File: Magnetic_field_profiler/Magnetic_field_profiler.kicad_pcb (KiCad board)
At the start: 4 copper layers, 92 x 37 mm, 71 parts, among them J1 USB_B_Micro, J2 Barrel_Jack_Switch, J3 Conn_01x04_Socket, Q1 BSS123, SW1 SW_SPDT, U1 STM32F103C8Tx, U10 MLX90393, U11 MLX90393, U12 MLX90393, U2 AP2112K-3.3, U3 DRV8825, U4 MLX90393, U5 MLX90393, U6 MLX90393, U7 MLX90393, U8 MLX90393, U9 MLX90393, Y1 Crystal_GND24

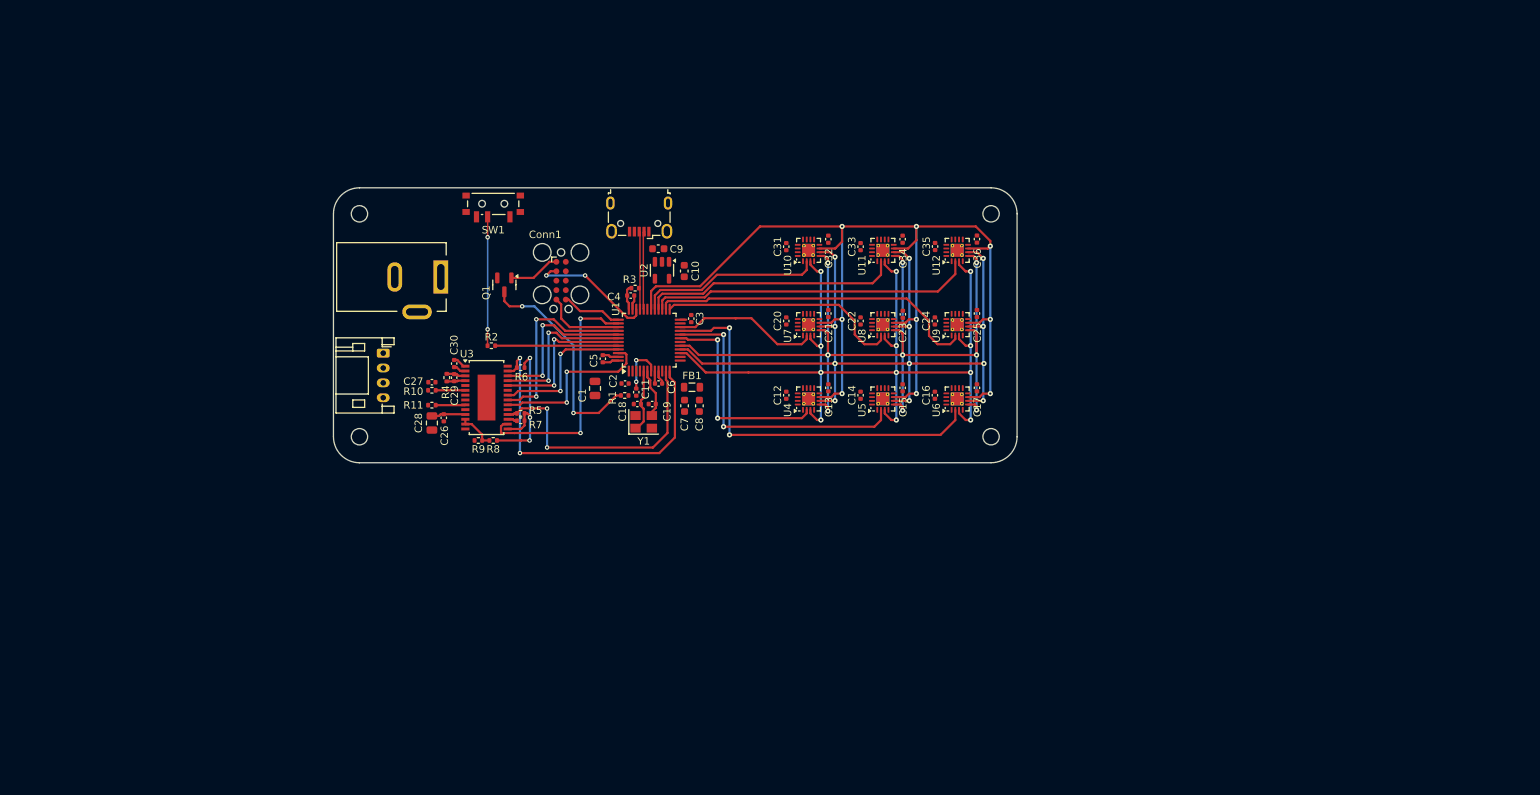
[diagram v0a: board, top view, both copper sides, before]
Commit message: SMPS Added, Edge Cuts Modified
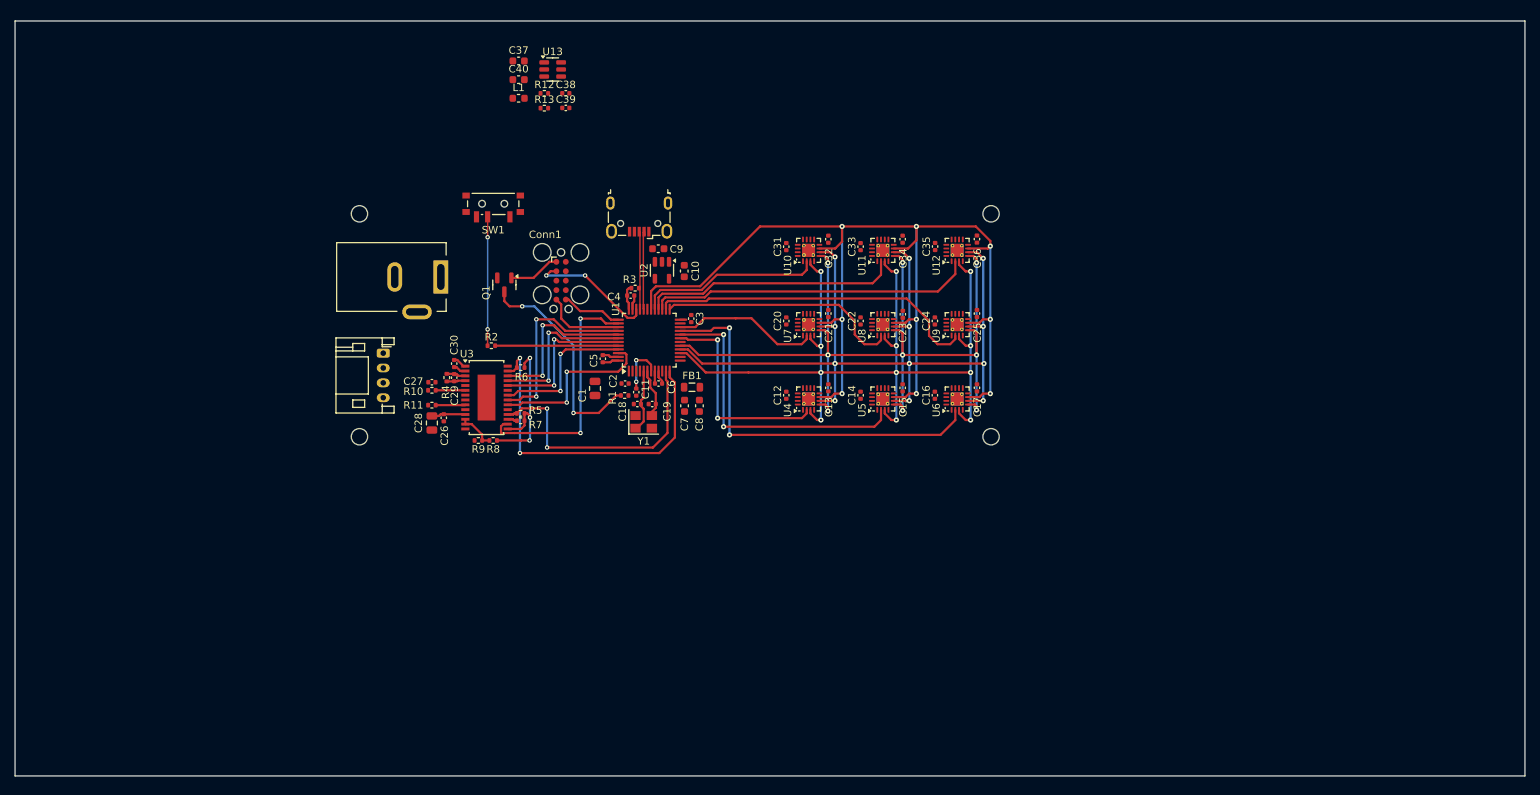
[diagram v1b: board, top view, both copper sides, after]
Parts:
- added C37: 22u, Capacitor_SMD:C_0603_1608Metric, F.Cu at (93.2, 56.2)
- added C38: 100n, Capacitor_SMD:C_0402_1005Metric, F.Cu at (99.5, 60.5)
- added C39: 100n, Capacitor_SMD:C_0402_1005Metric, F.Cu at (99.5, 62.5)
- added C40: 22u, Capacitor_SMD:C_0603_1608Metric, F.Cu at (93.2, 58.7)
- added L1: 100u, Inductor_SMD:L_0603_1608Metric, F.Cu at (93.2, 61.2)
- added R12: R, Resistor_SMD:R_0402_1005Metric, F.Cu at (96.6, 60.5)
- added R13: R, Resistor_SMD:R_0402_1005Metric, F.Cu at (96.6, 62.5)
- added U13: TP6841S6, Package_TO_SOT_SMD:SOT-23-6, F.Cu at (97.8, 57.3)
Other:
- board size 92 x 37 mm -> 203.2 x 101.6 mm

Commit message: Edge cuts updated
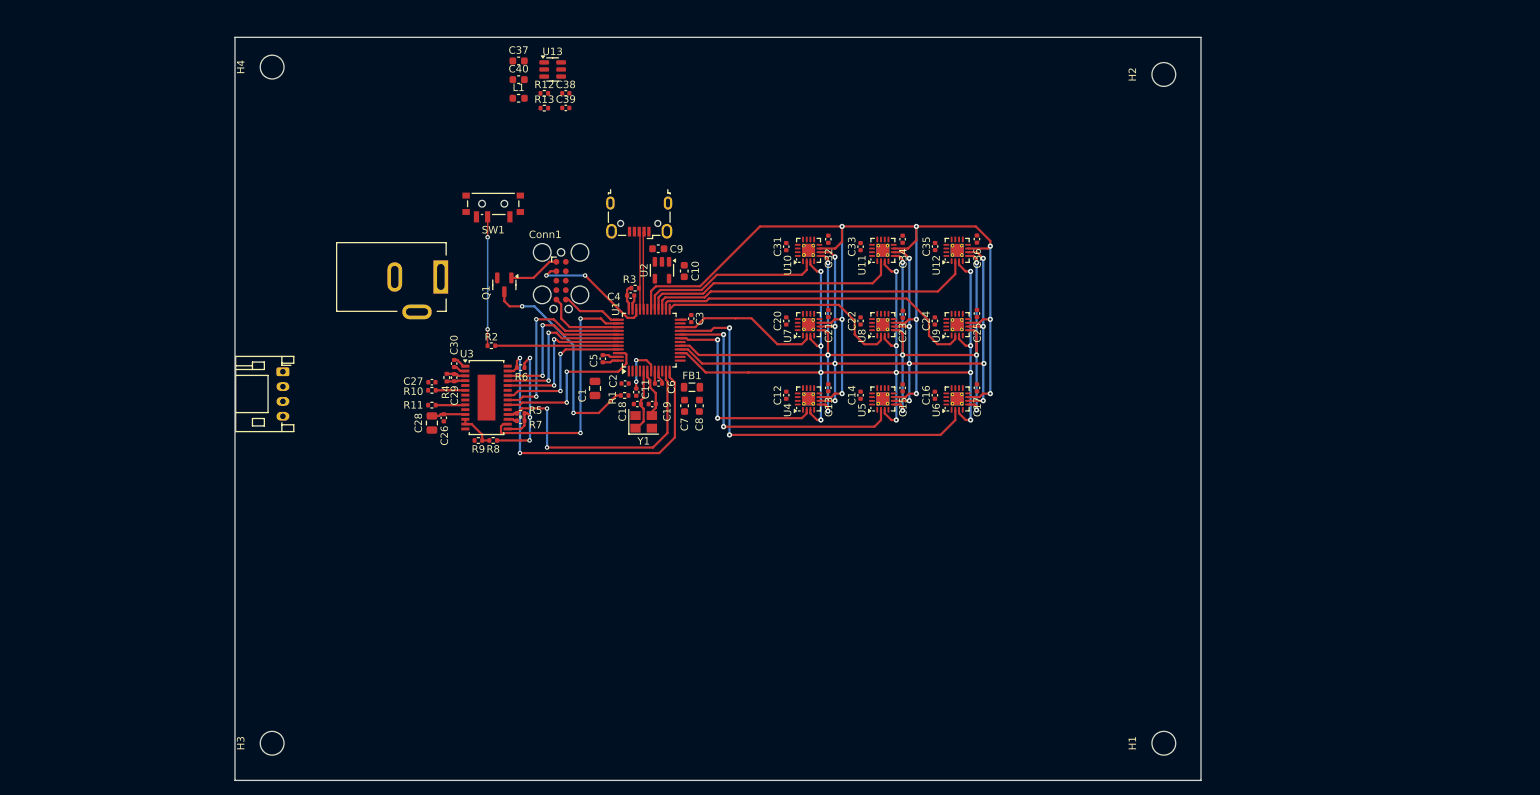
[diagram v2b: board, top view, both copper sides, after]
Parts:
- H1, H2, H3, H4: footprint MountingHole:MountingHole_2.2mm_M2 -> MountingHole:MountingHole_3.2mm_M3
- R12: value R -> 75k
- R13: value R -> 24k
- moved H1 47.4 mm to (180.0, 148.0)
- moved H3 42.9 mm to (60.0, 148.0)
- moved H2 29.9 mm to (180.0, 58.0)
- moved H4 23.0 mm to (60.0, 57.0)
- moved J3 13.7 mm to (61.5, 98.0)
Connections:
- C26 pad 1: +24V -> +12V
- C27 pad 1: +24V -> +12V
- C28 pad 1: +24V -> +12V
- C29 pad 1: +24V -> +12V
- R4 pad 1: +24V -> +12V
- U3 pad 11: +24V -> +12V
- U3 pad 4: +24V -> +12V
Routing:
- net +24V: track 7.15 -> 0.00 mm
- net +12V: track 0.00 -> 7.15 mm
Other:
- board size 203.2 x 101.6 mm -> 130 x 100 mm

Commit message: PCB Updates and Second Motor Support
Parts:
- added C41: 100n, Capacitor_SMD:C_0402_1005Metric, F.Cu at (142.4, 121.5)
- added C42: 100n, Capacitor_SMD:C_0402_1005Metric, F.Cu at (152.5, 126.8)
- added C43: 100n, Capacitor_SMD:C_0402_1005Metric, F.Cu at (152.5, 128.8)
- added J4: Screw_Terminal_01x06, TerminalBlock:TerminalBlock_Xinya_XY308-2.54-6P_1x06_P2.54mm_Horizontal, F.Cu at (60.0, 70.3)
- added R14: 1M, Resistor_SMD:R_0402_1005Metric, F.Cu at (119.5, 112.3)
- added R15: 10k, Resistor_SMD:R_0402_1005Metric, F.Cu at (119.5, 114.3)
- added R16: 10k, Resistor_SMD:R_0402_1005Metric, F.Cu at (119.5, 116.3)
- added R17: 10k, Resistor_SMD:R_0402_1005Metric, F.Cu at (119.5, 118.3)
- added R18: 50k, Resistor_SMD:R_0402_1005Metric, F.Cu at (119.5, 120.2)
- added R19: 30k, Resistor_SMD:R_0402_1005Metric, F.Cu at (119.5, 122.2)
- added R20: 200m, Resistor_SMD:R_0402_1005Metric, F.Cu at (119.5, 124.2)
- added R21: 200m, Resistor_SMD:R_0402_1005Metric, F.Cu at (119.5, 126.2)
- C10, C9: value 1u -> 100n; footprint Capacitor_SMD:C_0603_1608Metric -> Capacitor_SMD:C_0402_1005Metric
- C14: value 100n -> 100u; footprint Capacitor_SMD:C_0402_1005Metric -> Capacitor_SMD:C_0805_2012Metric
- C16: value 100n -> 10n
- J2: value Barrel_Jack_Switch -> Conn_01x04_Socket; footprint Connector_BarrelJack:BarrelJack_Kycon_KLDX-0202-xC_Horizontal -> Connector_JST:JST_PH_S4B-PH-K_1x04_P2.00mm_Horizontal
- U2: value AP2112K-3.3 -> MLX90393; footprint Package_TO_SOT_SMD:SOT-23-5 -> Package_DFN_QFN:QFN-16-1EP_3x3mm_P0.5mm_EP1.75x1.75mm_ThermalVias
- U4: value MLX90393 -> DRV8825; footprint Package_DFN_QFN:QFN-16-1EP_3x3mm_P0.5mm_EP1.75x1.75mm_ThermalVias -> Package_SO:TSSOP-28-1EP_4.4x9.7mm_P0.65mm
- moved C33 57.9 mm to (124.7, 137.2), turned to 0 degrees
- moved C31 56.4 mm to (142.4, 136.0), turned to 0 degrees
- moved C32 56.0 mm to (124.7, 135.3), turned to 0 degrees
- moved U9 55.2 mm to (120.6, 136.9), turned to 0 degrees
- moved J2 50.0 mm to (123.9, 113.7)
- moved C35 48.1 mm to (142.4, 128.8), turned to 0 degrees
- moved C21 47.3 mm to (152.5, 134.0), turned to 0 degrees
- moved U10 47.2 mm to (138.3, 128.4), turned to 0 degrees
- moved U12 46.9 mm to (148.5, 128.4), turned to 0 degrees
- moved C22 46.8 mm to (152.5, 136.0), turned to 0 degrees
- moved C34 46.7 mm to (142.4, 126.8), turned to 0 degrees
- moved C25 45.6 mm to (142.4, 134.0), turned to 0 degrees
- moved U8 44.2 mm to (138.3, 135.7), turned to 0 degrees
- moved C9 43.3 mm to (142.4, 112.3)
- moved C36 41.3 mm to (142.4, 119.5), turned to 0 degrees
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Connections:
- net /AOUT1 renamed /M1_AOUT1
- net /AOUT2 renamed /M1_AOUT2
- net /BOUT1 renamed /M1_BOUT1
- net /BOUT2 renamed /M1_BOUT2
- net /MTR_DIR renamed /MTR1_DIR
- net /MTR_NFAULT renamed /MTR1_NFAULT
- net /MTR_NHOME renamed /MTR1_NHOME
- net /MTR_STEP renamed /MTR1_STEP
- C12 pad 1: +3.3V -> +12V
- C13 pad 1: +3.3V -> +12V
- C14 pad 1: +3.3V -> +12V
- C15 pad 1: +3.3V -> +12V
- C15 pad 2: GND -> /VCP
- C16 pad 1: +3.3V -> /CP1
- C16 pad 2: GND -> /CP2
- C9 pad 1: +5V -> +3.3V
- J2 pad 1: +24V -> /M2_AOUT1
- J2 pad 2: GND -> /M2_AOUT2
- J2 pad 3: unconnected-(J2-Pad3) -> /M2_BOUT1
- R5 pad 1: /V3P3OUT -> /M1_V3P3OUT
- R6 pad 1: /V3P3OUT -> /M1_V3P3OUT
- U1 pad 13: unconnected-(U1-PA3-Pad13) -> /MTR2_NFAULT
- U1 pad 14: unconnected-(U1-PA4-Pad14) -> /MTR2_NHOME
- U1 pad 2: unconnected-(U1-PC13-Pad2) -> /MTR2_DIR
- U1 pad 3: unconnected-(U1-PC14-Pad3) -> /MTR2_STEP
- U10 pad 2: /MAG_CS7 -> /MAG_CS3
- U10 pad 3: /SPI.SPI_CLK -> /SPI.SPI_MISO
- U10 pad 5: /SPI.SPI_MOSI -> /SPI.SPI_CLK
- U10 pad 6: /SPI.SPI_MISO -> /SPI.SPI_MOSI
- U11 pad 2: /MAG_CS8 -> /MAG_CS6
- U11 pad 3: /SPI.SPI_CLK -> /SPI.SPI_MISO
- U11 pad 5: /SPI.SPI_MOSI -> /SPI.SPI_CLK
- U11 pad 6: /SPI.SPI_MISO -> /SPI.SPI_MOSI
- U12 pad 3: /SPI.SPI_CLK -> /SPI.SPI_MISO
- U12 pad 5: /SPI.SPI_MOSI -> /SPI.SPI_CLK
- U12 pad 6: /SPI.SPI_MISO -> /SPI.SPI_MOSI
- U2 pad 1: +5V -> unconnected-(U2-INT-Pad1)
- U2 pad 2: GND -> /MAG_CS1
- U2 pad 3: +5V -> /SPI.SPI_MISO
- U2 pad 5: +3.3V -> /SPI.SPI_CLK
- U3 pad 15: /V3P3OUT -> /M1_V3P3OUT
- U4 pad 1: unconnected-(U4-INT-Pad1) -> /CP1
- U4 pad 10: unconnected-(U4-NC-Pad10) -> /M2_BOUT1
- U4 pad 11: GND -> +12V
- U4 pad 12: GND -> /AVREF
- U4 pad 13: GND -> /AVREF
- U4 pad 14: unconnected-(U4-NC-Pad14) -> GND
- U4 pad 15: +3.3V -> /M2_V3P3OUT
- U4 pad 16: unconnected-(U4-NC-Pad16) -> /MTR_NRST
- U4 pad 17: GND -> /MTR_NSLEEP
- U4 pad 2: /MAG_CS1 -> /CP2
- U4 pad 3: /SPI.SPI_CLK -> /VCP
- U4 pad 4: unconnected-(U4-NC-Pad4) -> +12V
- U4 pad 5: /SPI.SPI_MOSI -> /M2_AOUT1
- U4 pad 6: /SPI.SPI_MISO -> /ISENA
- U4 pad 7: /MAG_TRIG -> /M2_AOUT2
- U4 pad 8: +3.3V -> /M2_BOUT2
- U4 pad 9: unconnected-(U4-NC-Pad9) -> /ISENB
- U5 pad 2: /MAG_CS2 -> /MAG_CS4
- U5 pad 3: /SPI.SPI_CLK -> /SPI.SPI_MISO
- U5 pad 5: /SPI.SPI_MOSI -> /SPI.SPI_CLK
- U5 pad 6: /SPI.SPI_MISO -> /SPI.SPI_MOSI
- U6 pad 2: /MAG_CS3 -> /MAG_CS7
- U6 pad 3: /SPI.SPI_CLK -> /SPI.SPI_MISO
- U6 pad 5: /SPI.SPI_MOSI -> /SPI.SPI_CLK
- U6 pad 6: /SPI.SPI_MISO -> /SPI.SPI_MOSI
- U7 pad 2: /MAG_CS4 -> /MAG_CS2
- U7 pad 3: /SPI.SPI_CLK -> /SPI.SPI_MISO
- U7 pad 5: /SPI.SPI_MOSI -> /SPI.SPI_CLK
- U7 pad 6: /SPI.SPI_MISO -> /SPI.SPI_MOSI
- U8 pad 3: /SPI.SPI_CLK -> /SPI.SPI_MISO
- U8 pad 5: /SPI.SPI_MOSI -> /SPI.SPI_CLK
- U8 pad 6: /SPI.SPI_MISO -> /SPI.SPI_MOSI
- U9 pad 2: /MAG_CS6 -> /MAG_CS8
- U9 pad 3: /SPI.SPI_CLK -> /SPI.SPI_MISO
- U9 pad 5: /SPI.SPI_MOSI -> /SPI.SPI_CLK
- U9 pad 6: /SPI.SPI_MISO -> /SPI.SPI_MOSI
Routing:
- net /MAG_TRIG: track 151.4 -> 9.31 mm, vias 9 -> 0
- net /SPI.SPI_MOSI: track 123.5 -> 3.02 mm, vias 9 -> 0
- net /SPI.SPI_CLK: track 121.7 -> 4.52 mm, vias 12 -> 0
- net /SPI.SPI_MISO: track 119.2 -> 3.73 mm, vias 12 -> 0
- net /MAG_CS3: track 53.9 -> 4.14 mm, vias 2 -> 0
- net /MAG_CS2: track 41.2 -> 0.00 mm, vias 2 -> 0
- net /MAG_CS6: track 44.5 -> 6.87 mm
- net /MAG_CS9: track 43.8 -> 8.21 mm
- net /MAG_CS5: track 32.8 -> 0.83 mm
- net /MAG_CS1: track 28.6 -> 1.12 mm, vias 2 -> 0
- net /MAG_CS8: track 34.6 -> 7.81 mm
- net /MAG_CS7: track 24.9 -> 8.46 mm
- net /MAG_CS4: track 19.9 -> 3.73 mm
